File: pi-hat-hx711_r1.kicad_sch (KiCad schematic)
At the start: 8 parts, among them J1 GPIO, J2 Conn_01x06, J5 Conn_01x06, U1 M24c64

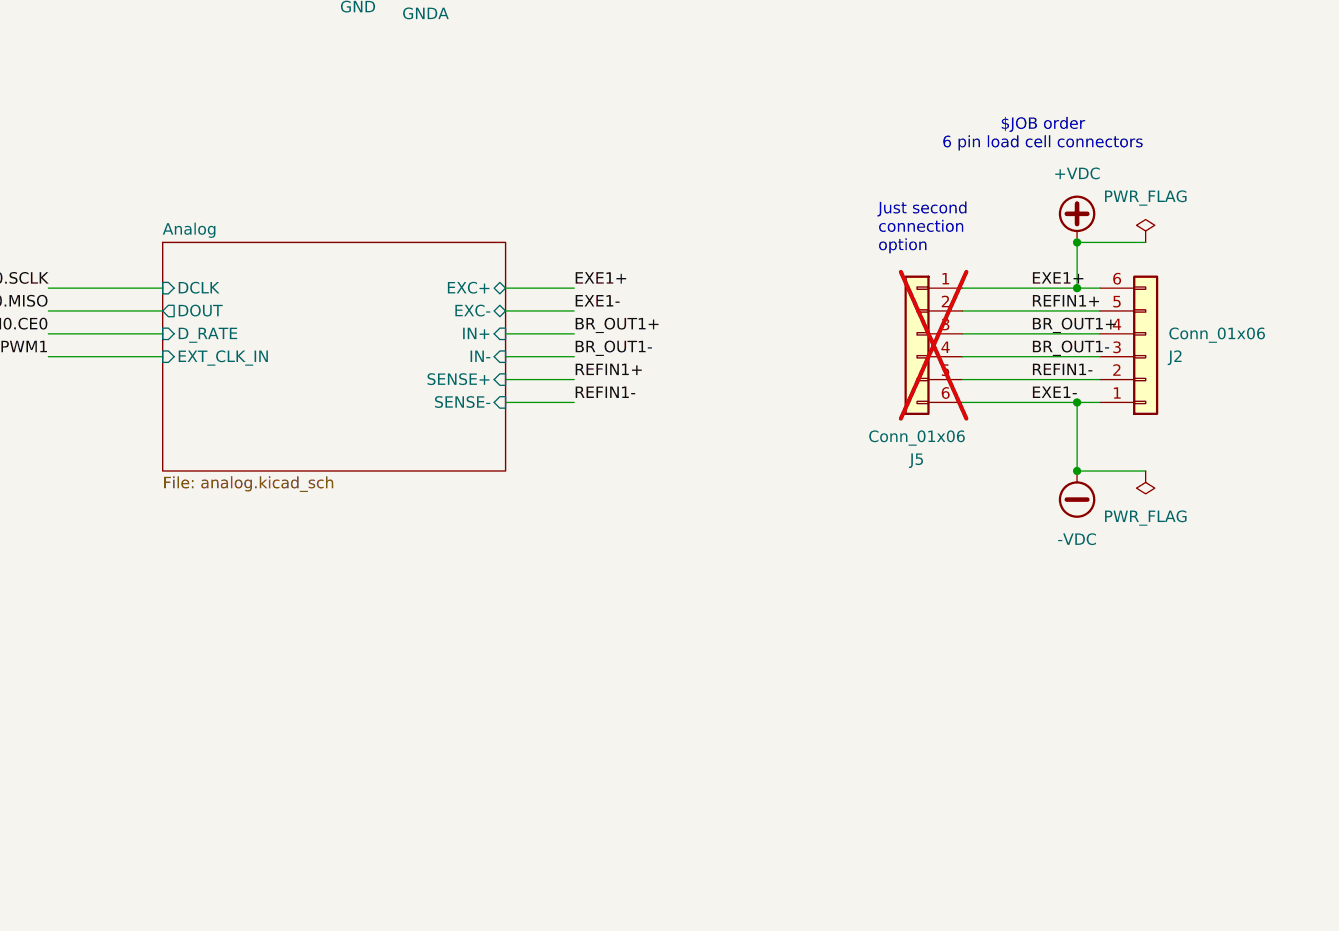
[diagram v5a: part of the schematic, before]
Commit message: add second channel input
switch to vertical connectors, so no concerns abotu edge space.
Allows offering the second channel, even though it's probably useless,
but it sets us up with a style we might be ok with for subsequent
boards.
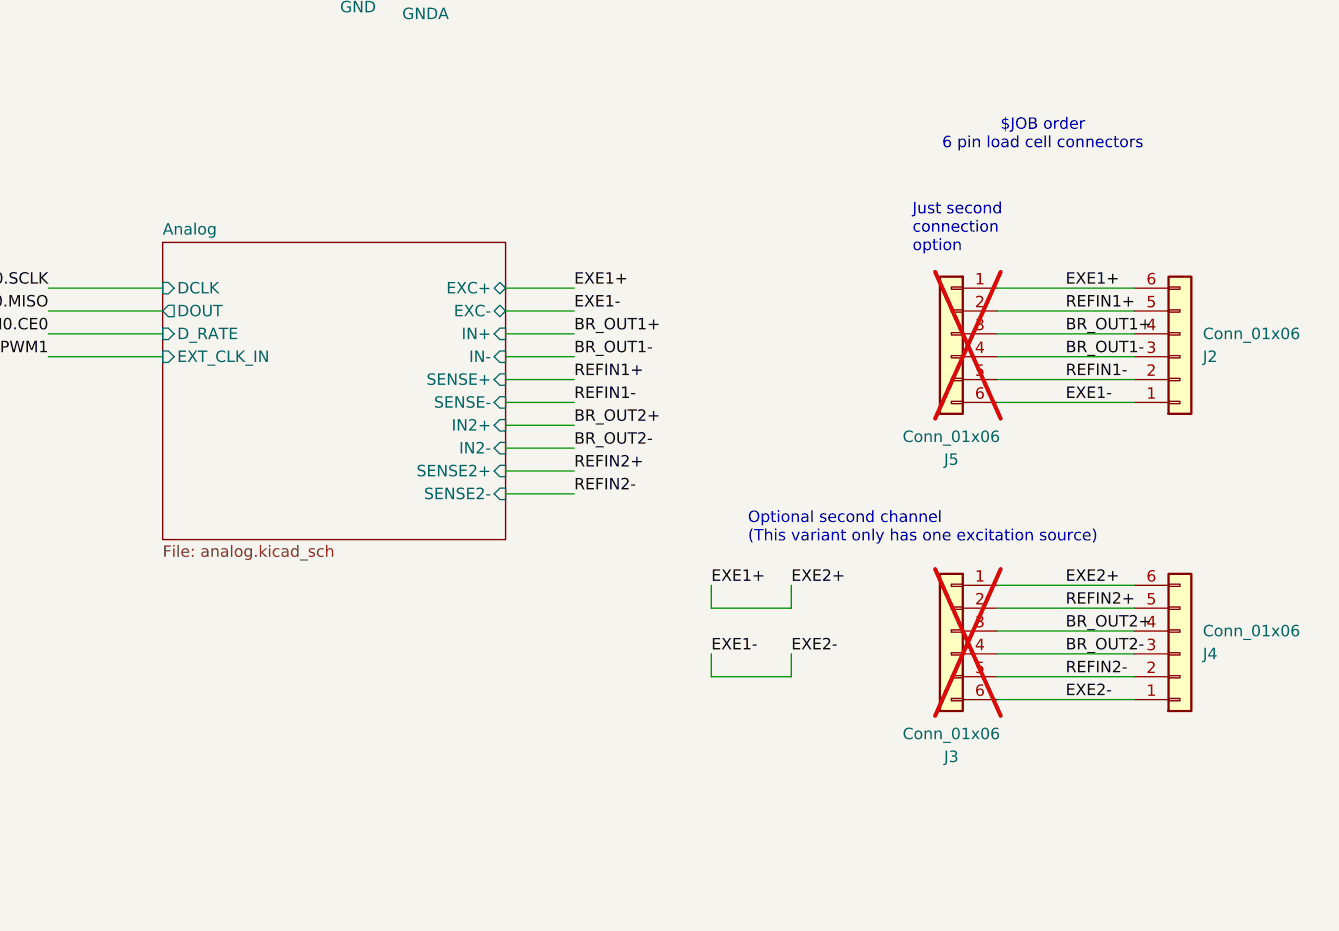
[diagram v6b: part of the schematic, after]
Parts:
- added J3: Conn_01x06, Connector_PinHeader_2.54mm:PinHeader_1x06_P2.54mm_Vertical, symbol Connector_Generic:Conn_01x06
- added J4: Conn_01x06, Connector_Phoenix_MC:PhoenixContact_MCV_1,5_6-G-3.81_1x06_P3.81mm_Vertical, symbol Connector_Generic:Conn_01x06
- J2: footprint Connector_Phoenix_MC:PhoenixContact_MC_1,5_6-G-3.81_1x06_P3.81mm_Horizontal -> Connector_Phoenix_MC:PhoenixContact_MCV_1,5_6-G-3.81_1x06_P3.81mm_Vertical; LCSC Part # C387811 -> C441336; MPN JL15EDGRC-38106G01 -> KF2EDGV-3.81-6P
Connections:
- net +VDC renamed EXE1+
- net EXE1+: now also J3.1 (Pin_1), J4.6 (Pin_6)
- net -VDC renamed EXE1-
- net EXE1-: now also J3.6 (Pin_6), J4.1 (Pin_1)
- new net BR_OUT2+: J3.3 (Pin_3), J4.4 (Pin_4)
- new net BR_OUT2-: J3.4 (Pin_4), J4.3 (Pin_3)
- new net REFIN2+: J3.2 (Pin_2), J4.5 (Pin_5)
- new net REFIN2-: J3.5 (Pin_5), J4.2 (Pin_2)
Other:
- sheet Analog ports: added IN2+, IN2-, SENSE2+, SENSE2-; removed none
- note added: "Optional second channel (This variant only has one excitation source)"
- moved on the sheet: J2, J5

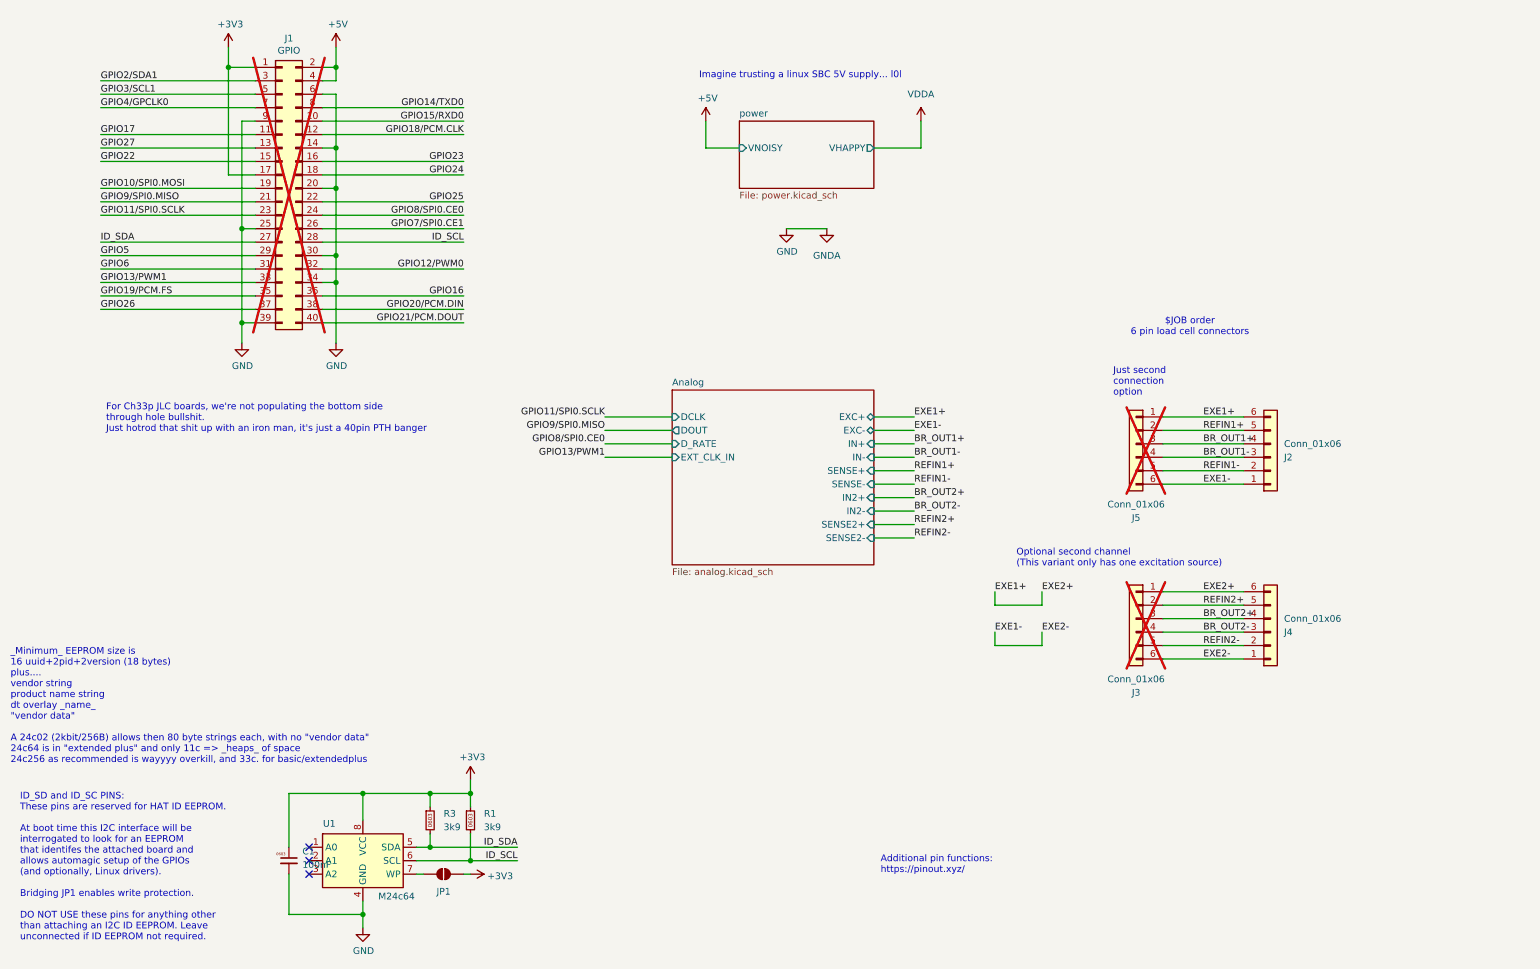
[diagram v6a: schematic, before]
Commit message: wheeww!
Added 3.3v supply from 5V by default.
Added header to access IOs without rpi
Added TP to supply/monitor raw 5V (use without pi)
Adjusted TPs to be on 2.54mm spacing to get headers if desired
Added TVS on EXE+ lines.
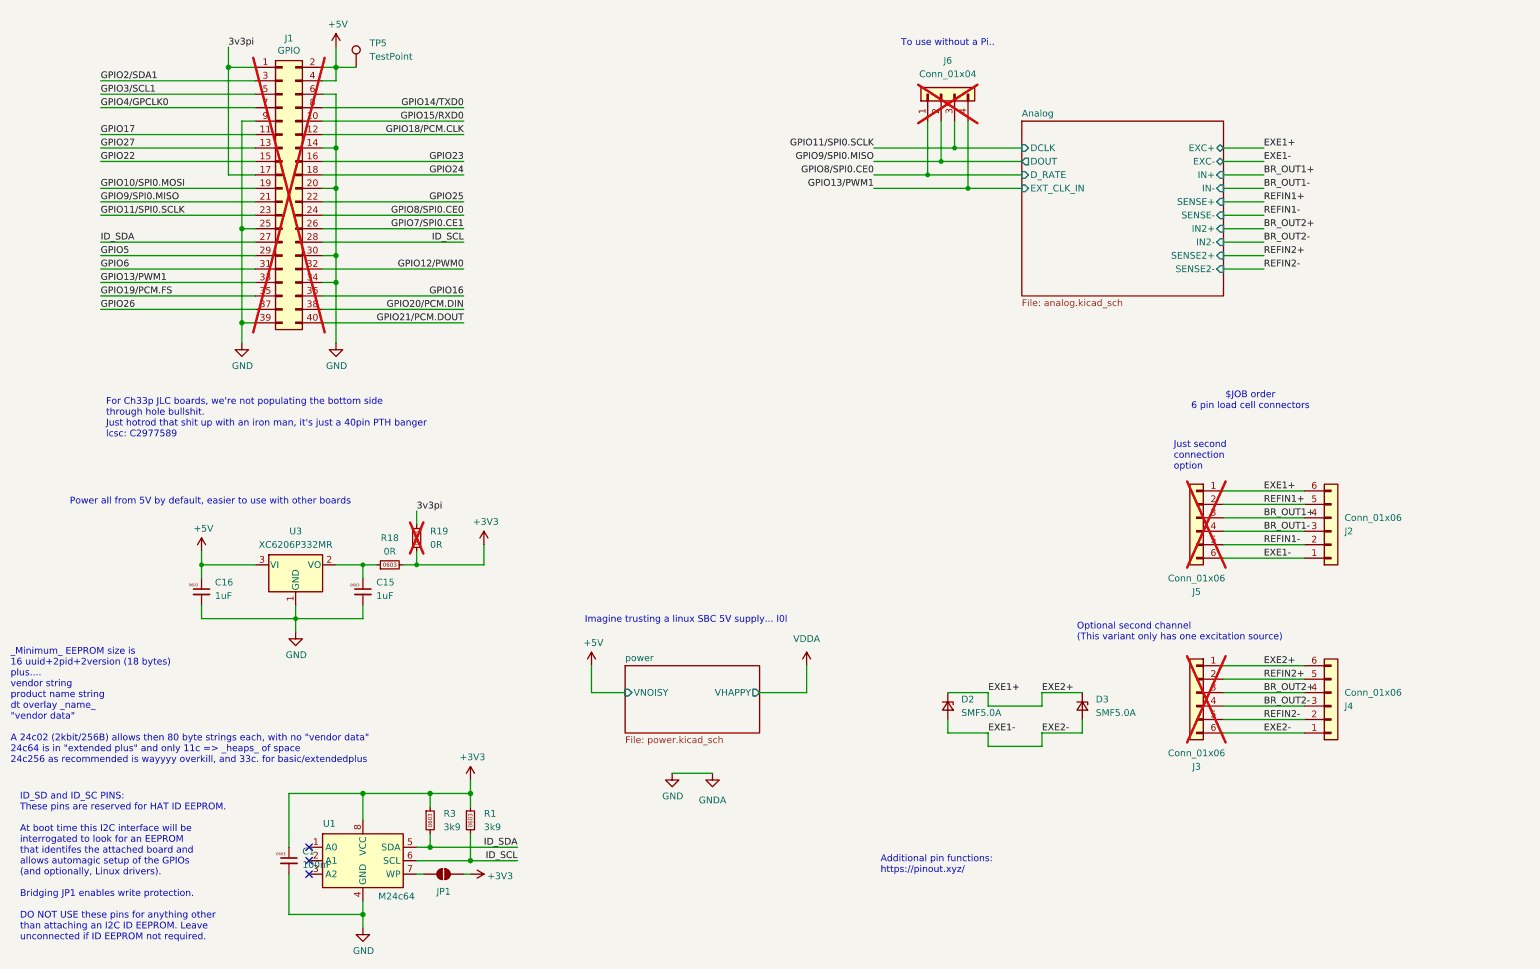
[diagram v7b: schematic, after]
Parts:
- added C15, C16: 1uF, Capacitor_SMD:C_0603_1608Metric, symbol karl-marel-atomics:KC0603_1uF
- added D2, D3: SMF5.0A, Diode_SMD:D_SOD-123F, symbol karl-marel-atomics:SMF5.0A
- added J6: Conn_01x04, Connector_PinHeader_2.54mm:PinHeader_1x04_P2.54mm_Vertical, symbol Connector_Generic:Conn_01x04
- added R18, R19: 0R, Resistor_SMD:R_0603_1608Metric, symbol karl-marel-atomics:KR0603_0R
- added TP5: TestPoint, TestPoint:TestPoint_THTPad_2.0x2.0mm_Drill1.0mm, symbol Connector:TestPoint
- added U3: XC6206P332MR, Package_TO_SOT_SMD:SOT-23-3, symbol Regulator_Linear:XC6206PxxxMR
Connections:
- net +3V3: now also R18.2, R19.1; no longer J1.1 (Pin_1), J1.17 (Pin_17)
- net +5V: now also C16.1, TP5.1, U3.3 (VI)
- net EXE1+: now also D2.1 (K), D3.1 (K)
- net EXE1-: now also D2.2 (A), D3.2 (A)
- net GND: now also C15.2, C16.2, U3.1 (GND)
- net GPIO11/SPI0.SCLK: now also J6.3 (Pin_3)
- net GPIO13/PWM1: now also J6.4 (Pin_4)
- net GPIO8/SPI0.CE0: now also J6.1 (Pin_1)
- net GPIO9/SPI0.MISO: now also J6.2 (Pin_2)
- new net: C15.1, R18.1, U3.2 (VO)
- new net 3v3pi: J1.1 (Pin_1), J1.17 (Pin_17), R19.2
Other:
- note added: "For Ch33p JLC boards, we're not populating the bottom side through hole bullshit. Just hotrod that shit up with an iron man, it's just a 40pin PTH banger lcsc: C2977589"
- note added: "Power all from 5V by default, easier to use with other boards"
- note added: "To use without a Pi.."
- note removed: "For Ch33p JLC boards, we're not populating the bottom side through hole bullshit. Just hotrod that shit up with an iron man, it's just a 40pin PTH banger"
- moved on the sheet: J2, J3, J4, J5

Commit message: erc/drc cleanups
fix lots of off grid stuff that got dragged off in earlier
re-arrangements
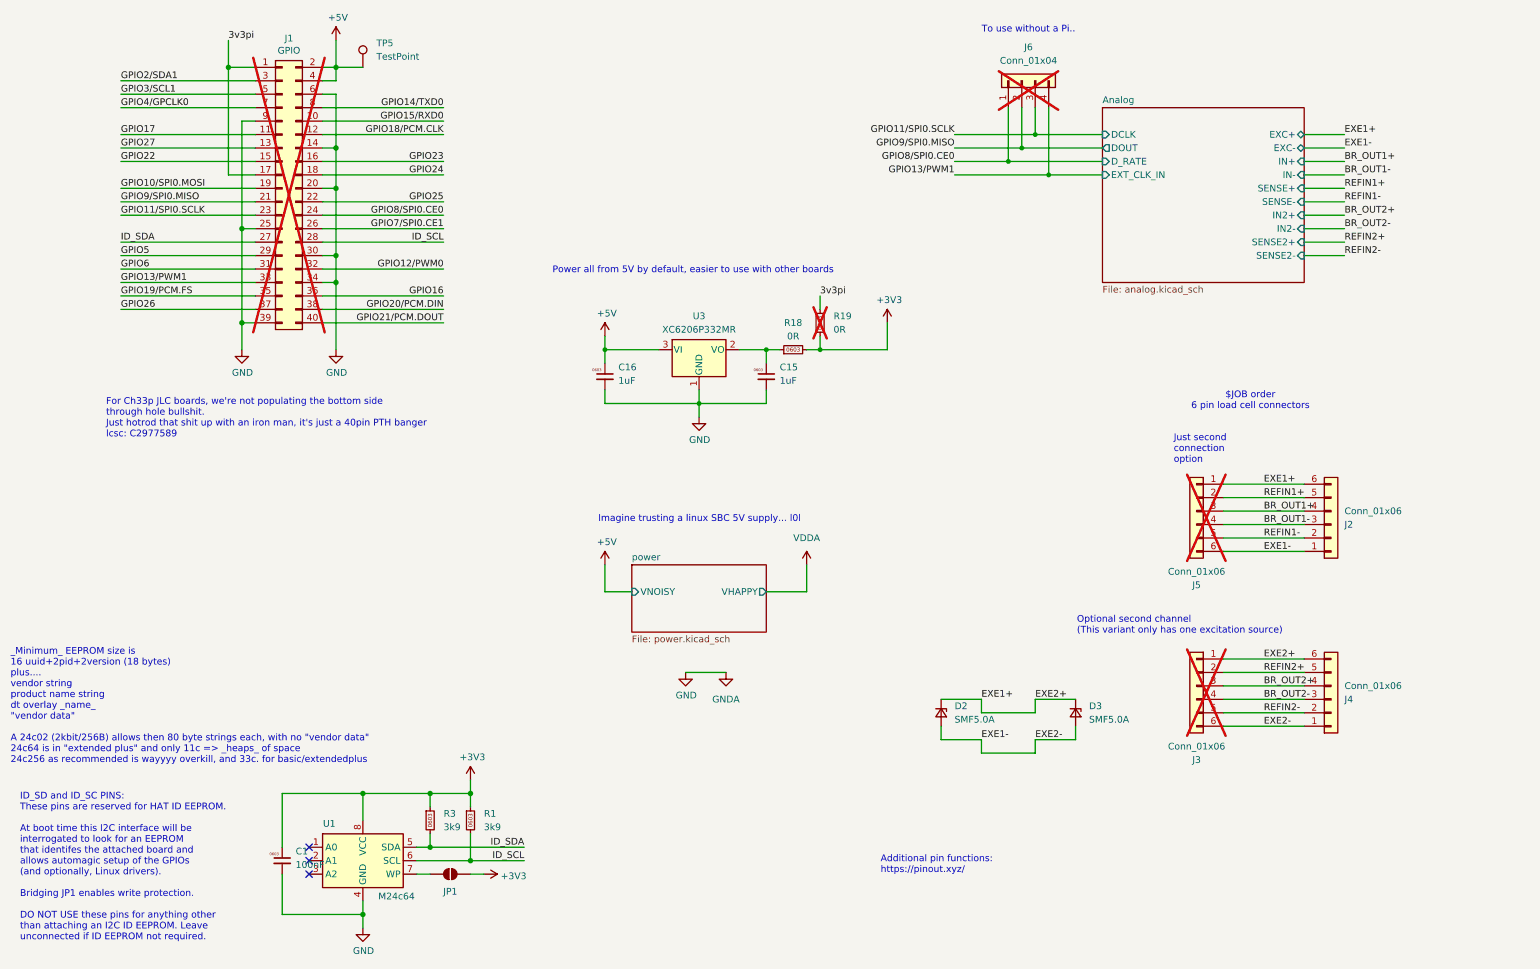
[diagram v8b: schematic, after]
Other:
- title: (none) -> HX711 Linux IIO Eval PiHAT
- moved on the sheet: C1, C15, C16, D2, D3, J2, J3, J4, J5, J6, JP1, R18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
